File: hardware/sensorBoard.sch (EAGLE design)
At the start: 35 parts, among them IC1 LM35CZ

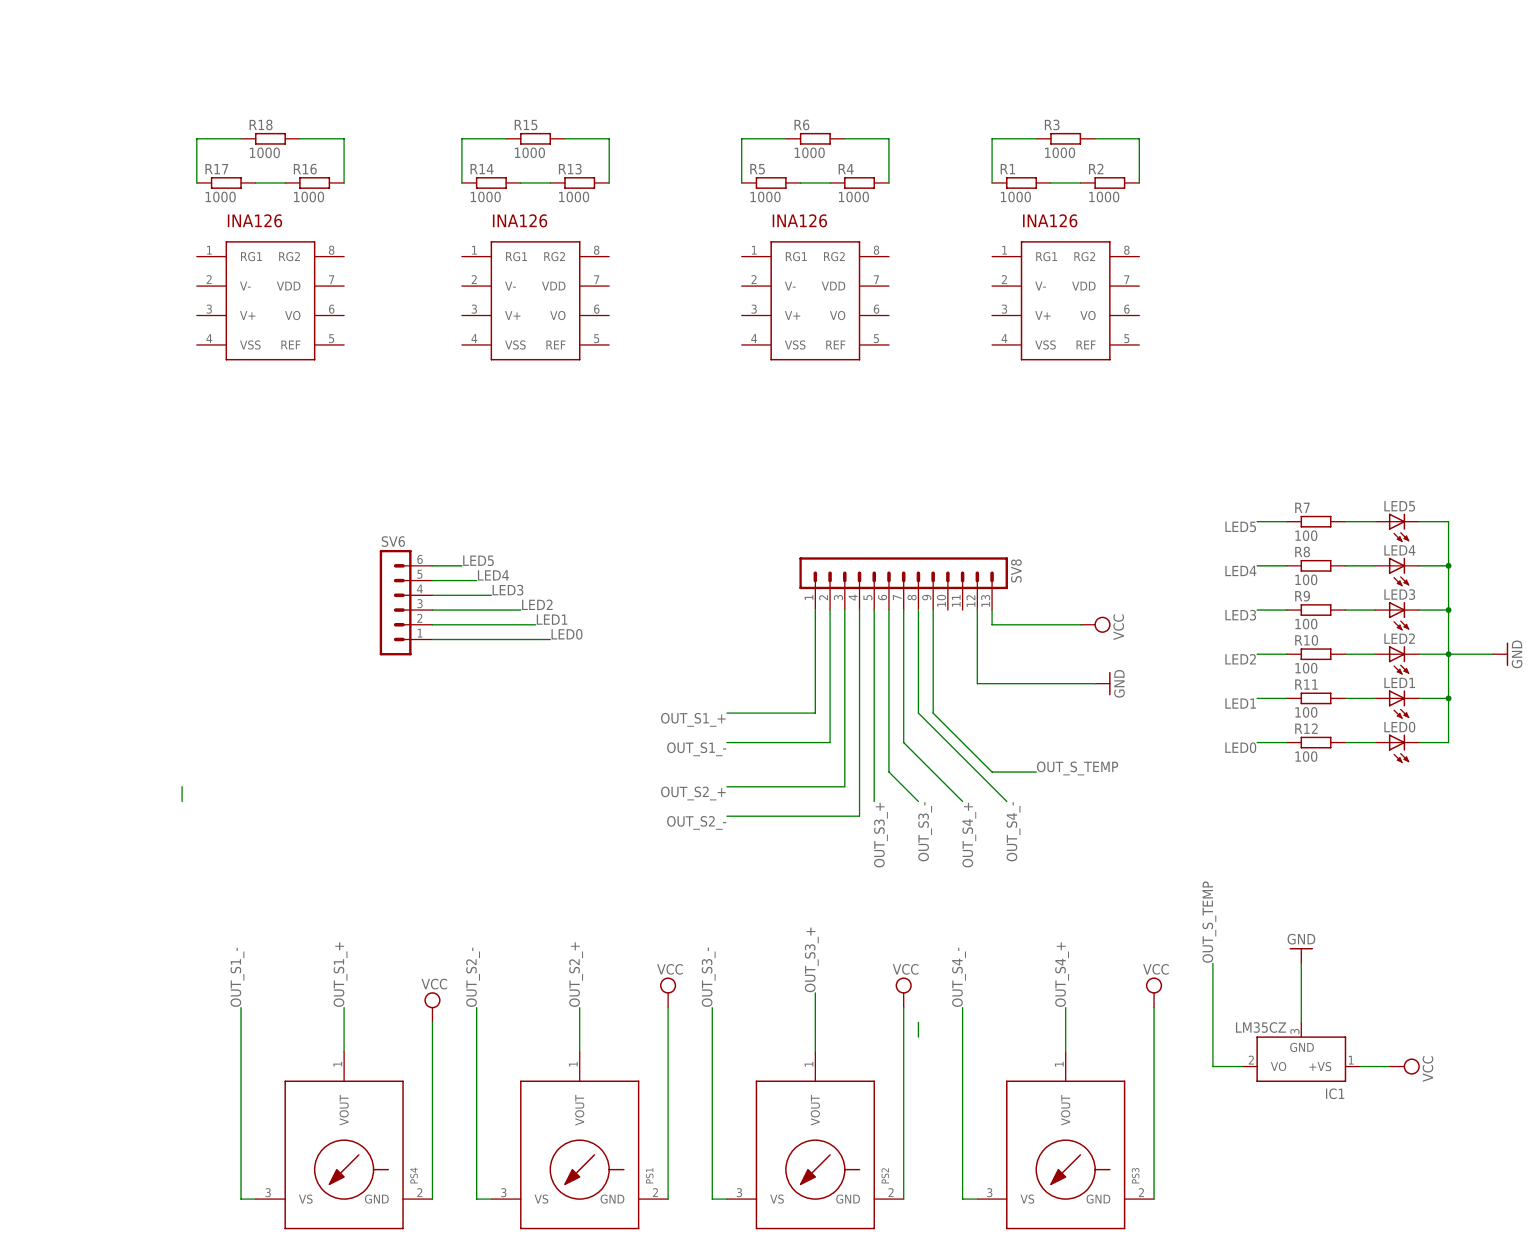
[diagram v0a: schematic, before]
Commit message: wired amplifier and start to set up SPI for ADC in schematic
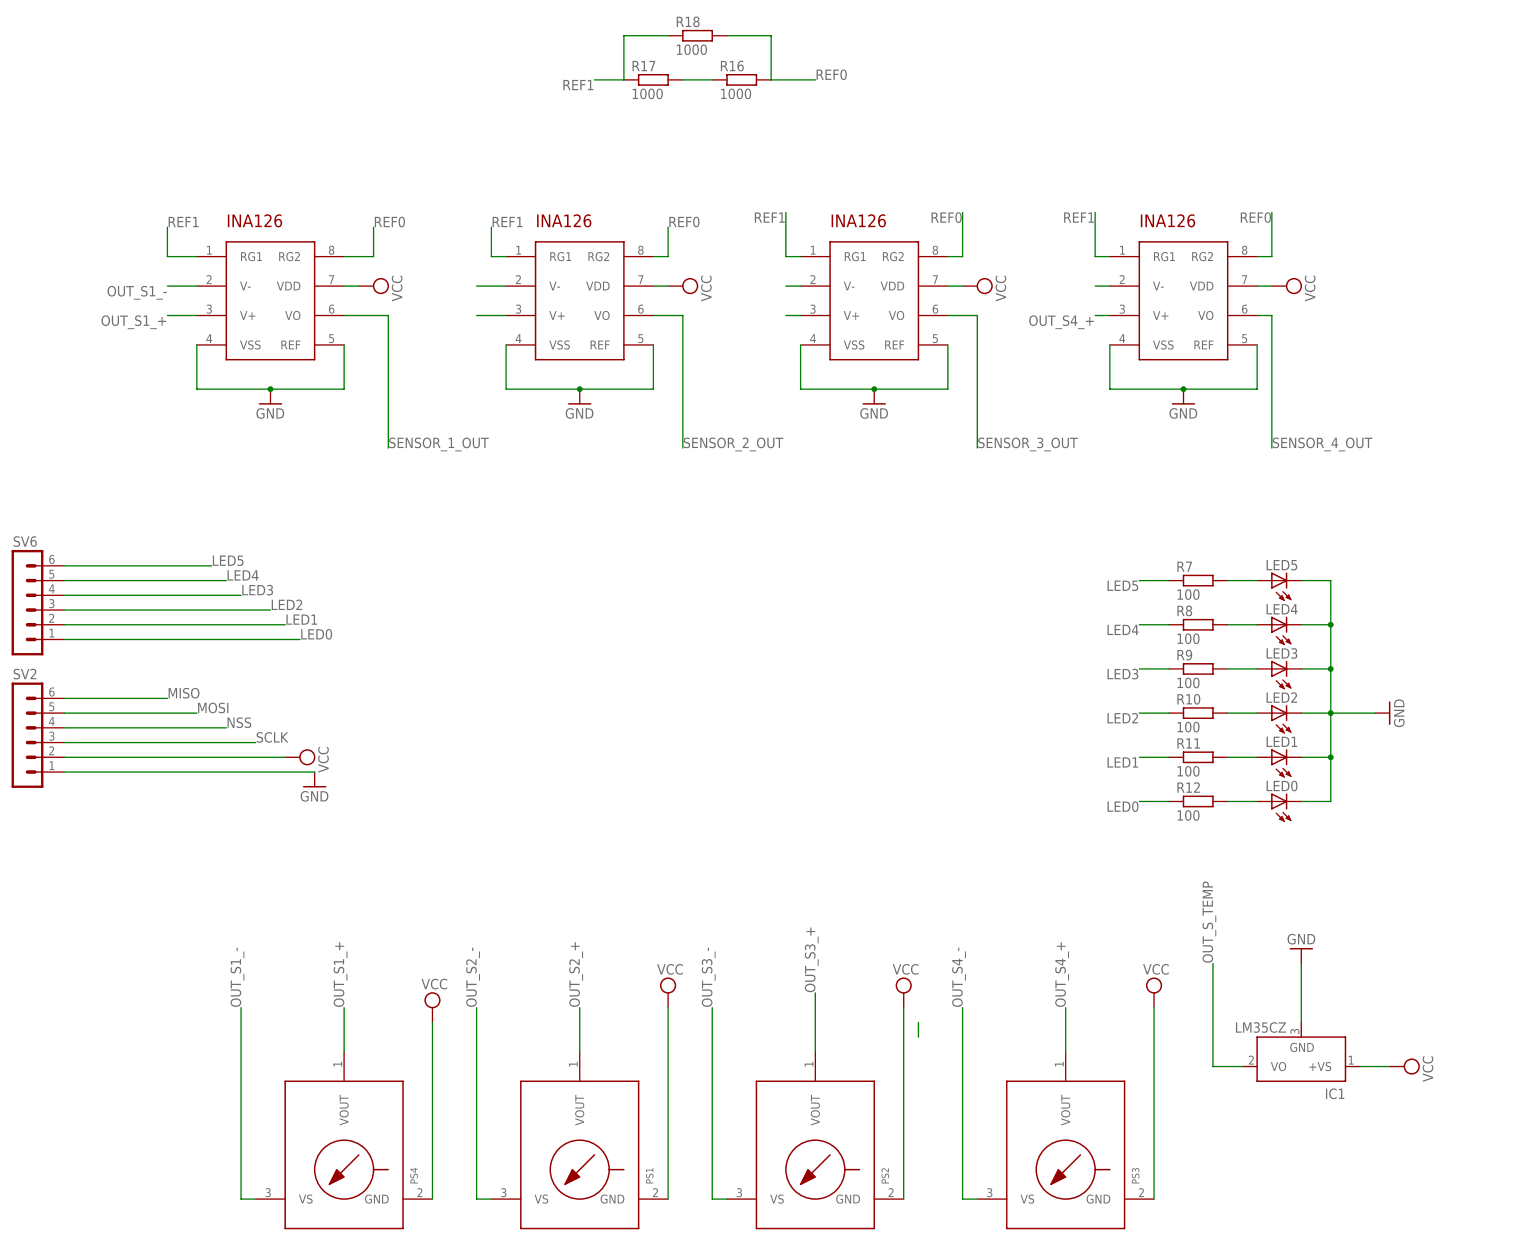
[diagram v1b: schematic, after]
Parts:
- removed R1, R13, R14, R15, R2, R3, R4, R5, R6: 1000, eagle-ltspice:R0207/10
- removed SV8: (no value), con-lstb:MA13-1
- added SV2: (no value), con-lstb:MA06-1
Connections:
- net N$10 renamed REF1
- removed net N$14: R1.2, R2.1
- removed net N$9: R18.2
- new net MISO: SV2.6
- new net MOSI: SV2.5
- new net N$1: U$4.RG2
- new net N$16: U$4.V-
- new net N$18: U$4.V+
- new net N$19: U$2.RG1
- new net N$24: U$2.RG2
- new net N$26: U$3.RG1
- new net N$27: U$3.RG2
- new net N$28: U$3.V-
- new net N$29: U$3.V+
- new net N$4: U$1.V+
- new net NSS: SV2.4
- new net REF0: R16.2, R18.2
- new net SCLK: SV2.3
- new net SENSOR_1_OUT: U$4.VO
- new net SENSOR_2_OUT: U$1.VO
- new net SENSOR_3_OUT: U$2.VO
- new net SENSOR_4_OUT: U$3.VO
- net GND: now also SV2.1, U$1.REF, U$1.VSS, U$2.REF, U$2.VSS, U$3.REF, U$3.VSS, U$4.REF, U$4.VSS; no longer SV8.12
- net N$12: now also U$2.V-; no longer R13.1, R14.2
- net N$13: now also U$2.V+; no longer R4.1, R5.2
- net N$2: now also U$4.RG1; no longer R15.2
- net N$3: now also U$1.V-; no longer R6.1
- net N$5: now also U$1.RG1; no longer R1.1, R3.1
- net N$7: now also U$1.RG2; no longer R2.2, R3.2
- net OUT_S1_+: no longer SV8.1
- net OUT_S1_-: no longer SV8.2
- net OUT_S2_+: no longer SV8.3
- net OUT_S2_-: no longer SV8.4
- net OUT_S3_+: no longer SV8.5
- net OUT_S3_-: no longer SV8.6
- net OUT_S4_+: no longer SV8.7
- net OUT_S4_-: no longer SV8.8
- net OUT_S_TEMP: no longer SV8.9
- net VCC: now also SV2.2, U$1.VDD, U$2.VDD, U$3.VDD, U$4.VDD; no longer SV8.13
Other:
- moved on the sheet: LED0, LED1, LED2, LED3, LED4, LED5, R10, R11, R12, R16, R17, R18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

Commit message: build sensor sandwich board to get it smaller. Still waiting for the ADC we would like to use
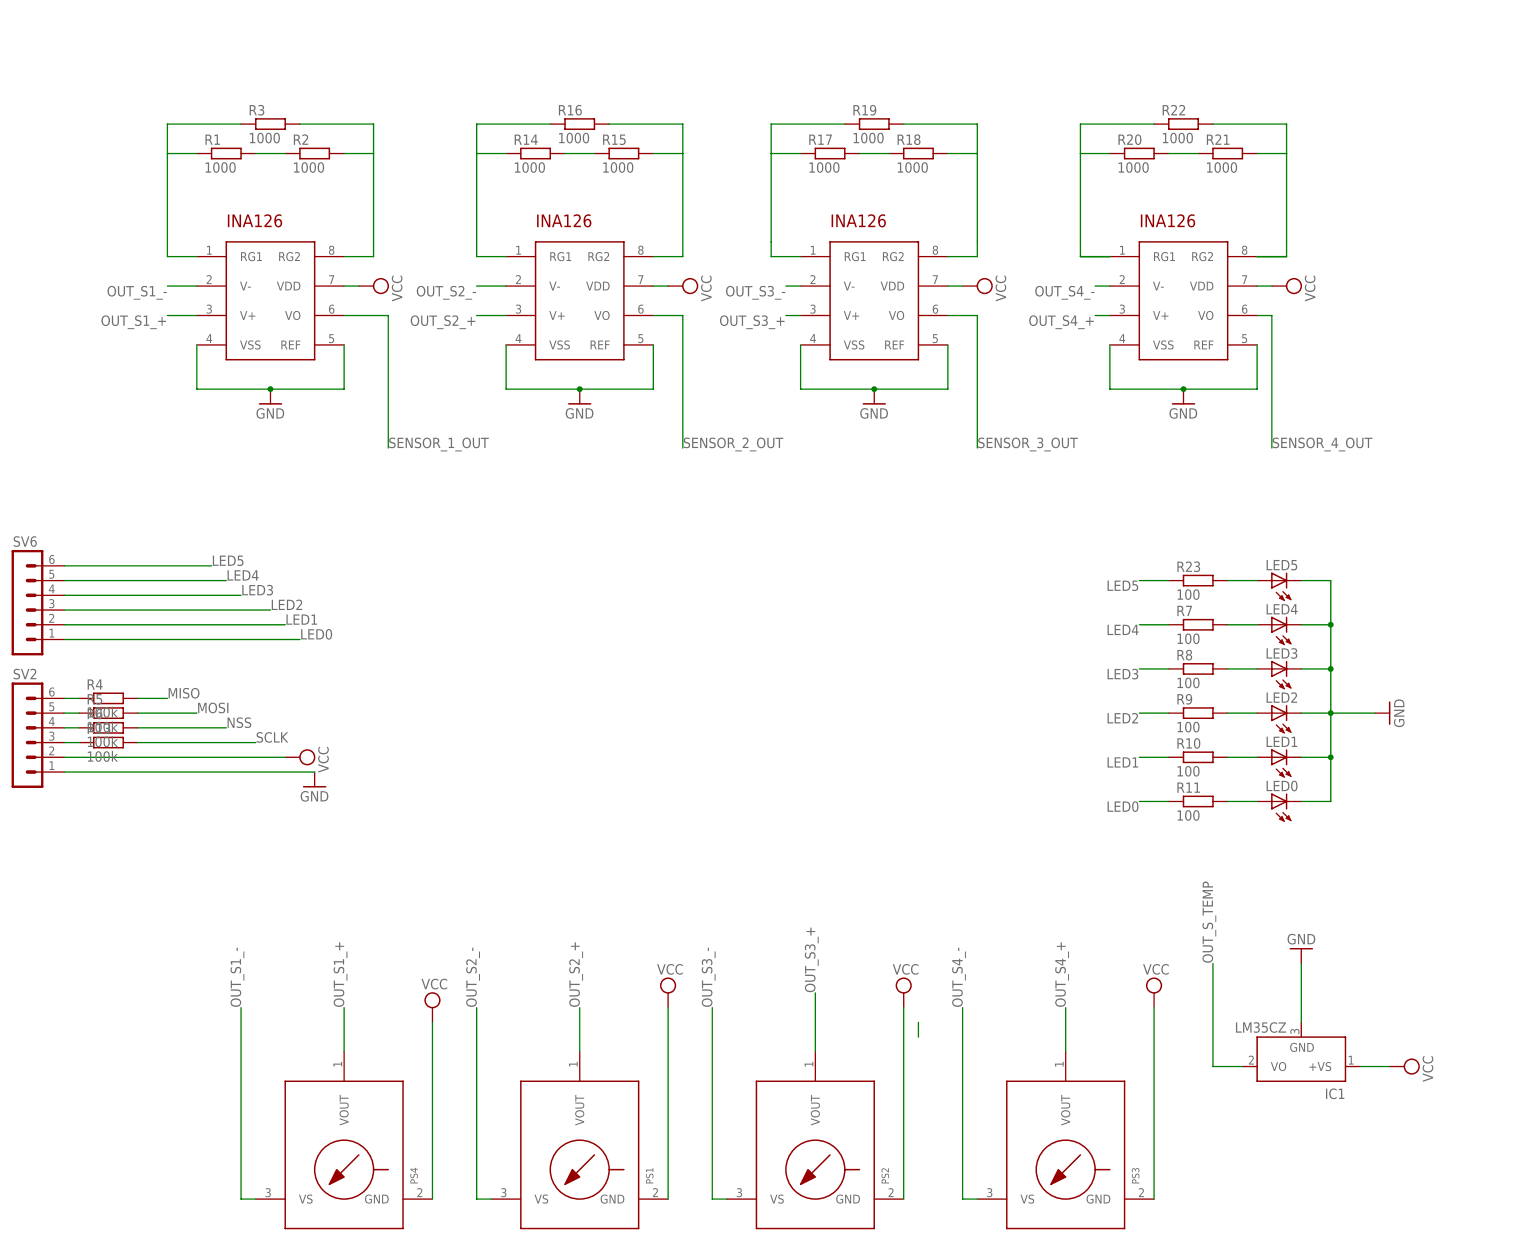
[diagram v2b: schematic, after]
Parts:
- removed R12: 100, eagle-ltspice:R0207/10
- added R1, R14, R15, R19, R2, R20, R21, R22, R3: 1000, rcl:R-EU_R0603
- added R13, R4, R5, R6: 100k, rcl:R-EU_R0603
- added R23: 100, rcl:R-EU_R0603
- R10, R11, R16, R17, R18, R7, R8, R9: device eagle-ltspice:R0207/10 -> rcl:R-EU_R0603
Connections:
- removed net REF0: R16.2, R18.2
- removed net REF1: R17.1, R18.1
- new net N$10: R14.1, R16.1
- new net N$30: R17.2, R18.1
- new net N$35: R20.2, R21.1
- new net N$8: R1.2, R2.1
- net LED0: now also R11.1; no longer R12.1
- net LED1: now also R10.1; no longer R11.1
- net LED2: now also R9.1; no longer R10.1
- net LED3: now also R8.1; no longer R9.1
- net LED4: now also R7.1; no longer R8.1
- net LED5: now also R23.1; no longer R7.1
- net MISO: now also R4.1, R4.2
- net MOSI: now also R5.1, R5.2
- net N$1: now also R2.2, R3.2
- net N$11: now also R14.2, R15.1; no longer R16.1, R17.2
- net N$17: now also R7.2; no longer R8.2
- net N$19: now also R17.1, R19.1
- net N$2: now also R1.1, R3.1
- net N$20: now also R8.2; no longer R9.2
- net N$21: now also R9.2; no longer R10.2
- net N$22: now also R10.2; no longer R11.2
- net N$23: now also R11.2; no longer R12.2
- net N$24: now also R18.2, R19.2
- net N$26: now also R20.1, R22.1
- net N$27: now also R21.2, R22.2
- net N$6: now also R23.2; no longer R7.2
- net N$7: now also R15.2, R16.2
- net NSS: now also R6.1, R6.2
- net SCLK: now also R13.1, R13.2
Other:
- moved on the sheet: R10, R11, R16, R17, R18, R7, R8, R9
